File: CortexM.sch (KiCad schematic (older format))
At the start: 8 parts

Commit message: Finish sch without values
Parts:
- added C10, C11, C3, C4, C5, C6, C7, C8, C9: C_Small, symbol Device:C_Small
- added D2: LED, symbol Device:LED
- added J2, J3: Conn_01x15, symbol Connector_Generic:Conn_01x15
- added JP1: SolderJumper_2_Open, symbol Jumper:SolderJumper_2_Open
- added L1: L_Small, symbol Device:L_Small
- added R2, R3: R_Small, symbol Device:R_Small
- added Y1: Crystal_Small, symbol Device:Crystal_Small
- gave numbers to parts that had none: 8
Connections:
- net +3V3: now also U2.1 (VBAT), U2.24 (VDD), U2.36 (VDD), U2.48 (VDD), C3.1, C4.1, C6.1, C8.1, C9.1, J2.1 (Pin_1), J3.1 (Pin_1), JP1.1 (A), L1.1, R3.1
- net GND: now also U2.23 (VSS), U2.35 (VSS), U2.47 (VSS), U2.8 (VSSA), C10.2, C11.2, C3.2, C4.2, C5.2, C6.2, C7.2, C8.2, C9.2, D2.1 (K), J2.2 (Pin_2), J3.2 (Pin_2), R2.2
- net USB_D+: now also U2.33 (PA12), R3.2
- net USB_D-: now also U2.32 (PA11)
- net LED_STAT: now reaches U2.11 (PA1)
- net LED_STAT: now also D2.2 (A)
- net PA3: now reaches U2.13 (PA3)
- net PA3: now also J3.15 (Pin_15)
- net PA4: now reaches U2.14 (PA4)
- net PA4: now also J3.14 (Pin_14)
- net PA5: now reaches U2.15 (PA5)
- net PA5: now also J3.13 (Pin_13)
- net PA6: now reaches U2.16 (PA6)
- net PA6: now also J3.12 (Pin_12)
- net PA7: now reaches U2.17 (PA7)
- net PA7: now also J3.11 (Pin_11)
- net PB0: now reaches U2.18 (PB0)
- net PB0: now also J3.10 (Pin_10)
- net PB1: now reaches U2.19 (PB1)
- net PB1: now also J3.9 (Pin_9)
- net PC13: now reaches U2.2 (PC13)
- net PC13: now also J2.13 (Pin_13)
- net PB2: now reaches U2.20 (PB2)
- net PB2: now also J3.8 (Pin_8)
- net PB10: now reaches U2.21 (PB10)
- net PB10: now also J3.7 (Pin_7)
- net PB11: now reaches U2.22 (PB11)
- net PB11: now also J3.6 (Pin_6)
- net PA8: now reaches U2.29 (PA8)
- net PA8: now also J3.5 (Pin_5)
- net PC14: now reaches U2.3 (PC14)
- net PC14: now also J2.14 (Pin_14)
- net PA9: now reaches U2.30 (PA9)
- net PA9: now also J3.4 (Pin_4)
- net PA10: now reaches U2.31 (PA10)
- net PA10: now also J3.3 (Pin_3)
- net SWDIO: now reaches U2.34 (PA13)
- net SWDIO: now also J2.3 (Pin_3)
- net SWCLK: now reaches U2.37 (PA14)
- net SWCLK: now also J2.4 (Pin_4)
- net PA15: now reaches U2.38 (PA15)
- net PA15: now also J2.5 (Pin_5)
- net SWO: now reaches U2.39 (PB3)
- net SWO: now also J2.6 (Pin_6)
- net PC15: now reaches U2.4 (PC15)
- net PC15: now also J2.15 (Pin_15)
- net PB4: now reaches U2.40 (PB4)
- net PB4: now also J2.7 (Pin_7)
- net PB5: now reaches U2.41 (PB5)
- net PB5: now also J2.8 (Pin_8)
- net PB6: now reaches U2.42 (PB6)
- net PB6: now also J2.9 (Pin_9)
- net PB7: now reaches U2.43 (PB7)
- net PB7: now also J2.10 (Pin_10)
- net at U2.44 (BOOT0): now also JP1.2 (B), R2.1
- net PB8: now reaches U2.45 (PB8)
- net PB8: now also J2.11 (Pin_11)
- net PB9: now reaches U2.46 (PB9)
- net PB9: now also J2.12 (Pin_12)
- net at U2.5 (PD0): now also C5.1, Y1.1
- net at U2.6 (PD1): now also C7.1, Y1.2
- net +3.3VA: now reaches U2.9 (VDDA)
- net +3.3VA: now also C10.1, C11.1, L1.2
- no-connect marks 2 -> 9
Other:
- note added: "'Light' low-pass filter for analog VDD"
- note added: "1x bulk decoupling + 100nF per VDD pin"
- note added: "BOOT0:\n1 = BOOTLOADER, 0='RUN'"
- note added: "CL = 2 * (Cload - Cstray)"
- note added: "GPIO HEADERS"
- note added: "STM32F1 Microcontroller"
- note added: "STM32F103"
- moved on the sheet: C1, C2, D1, FB1, J1, R1, U1, U2

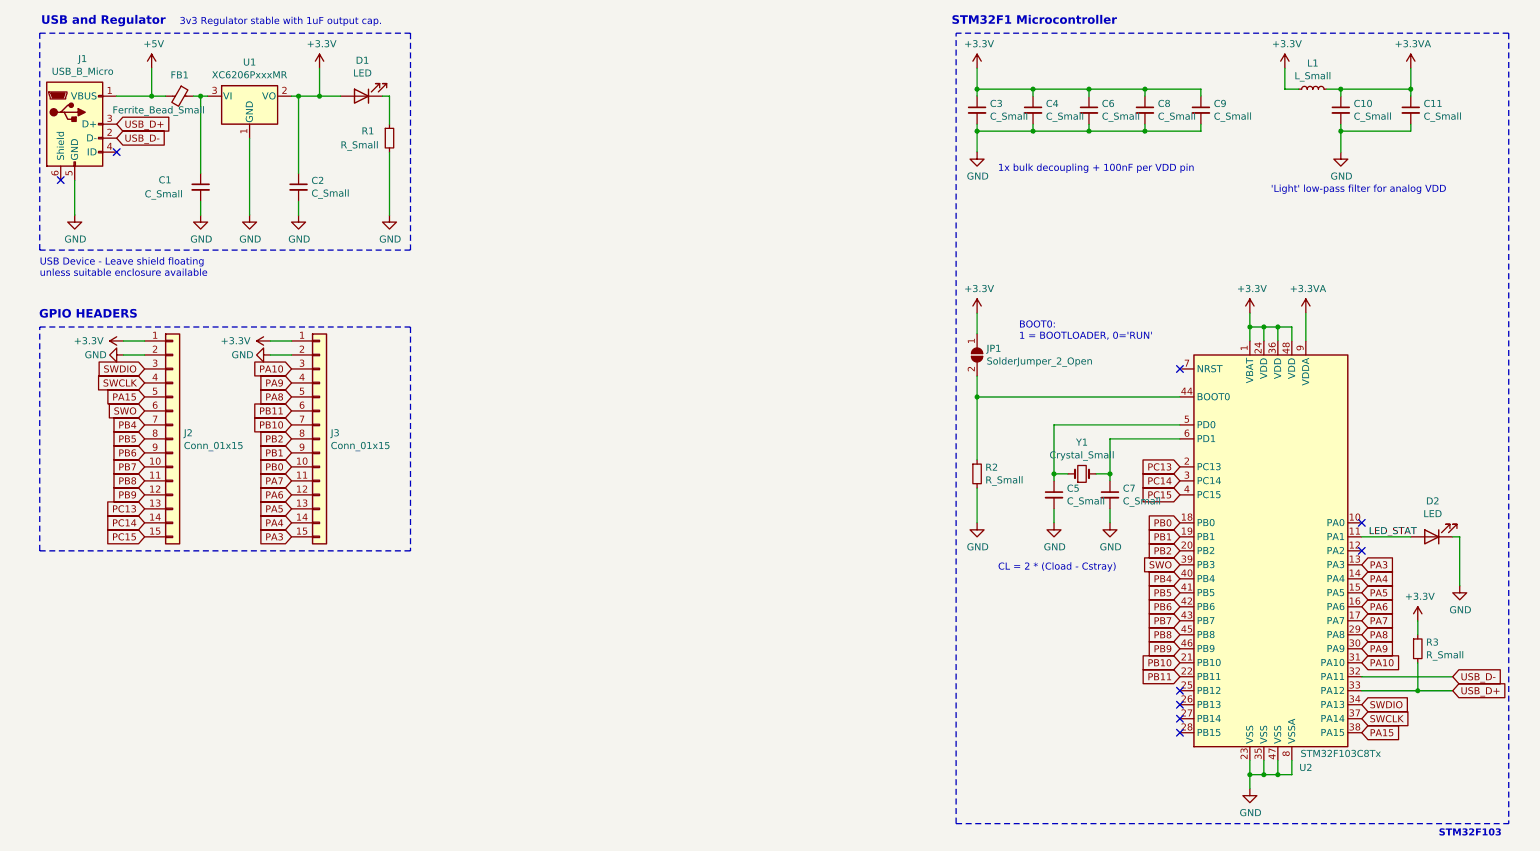
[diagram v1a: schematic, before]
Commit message: Added R4, Added values to sch
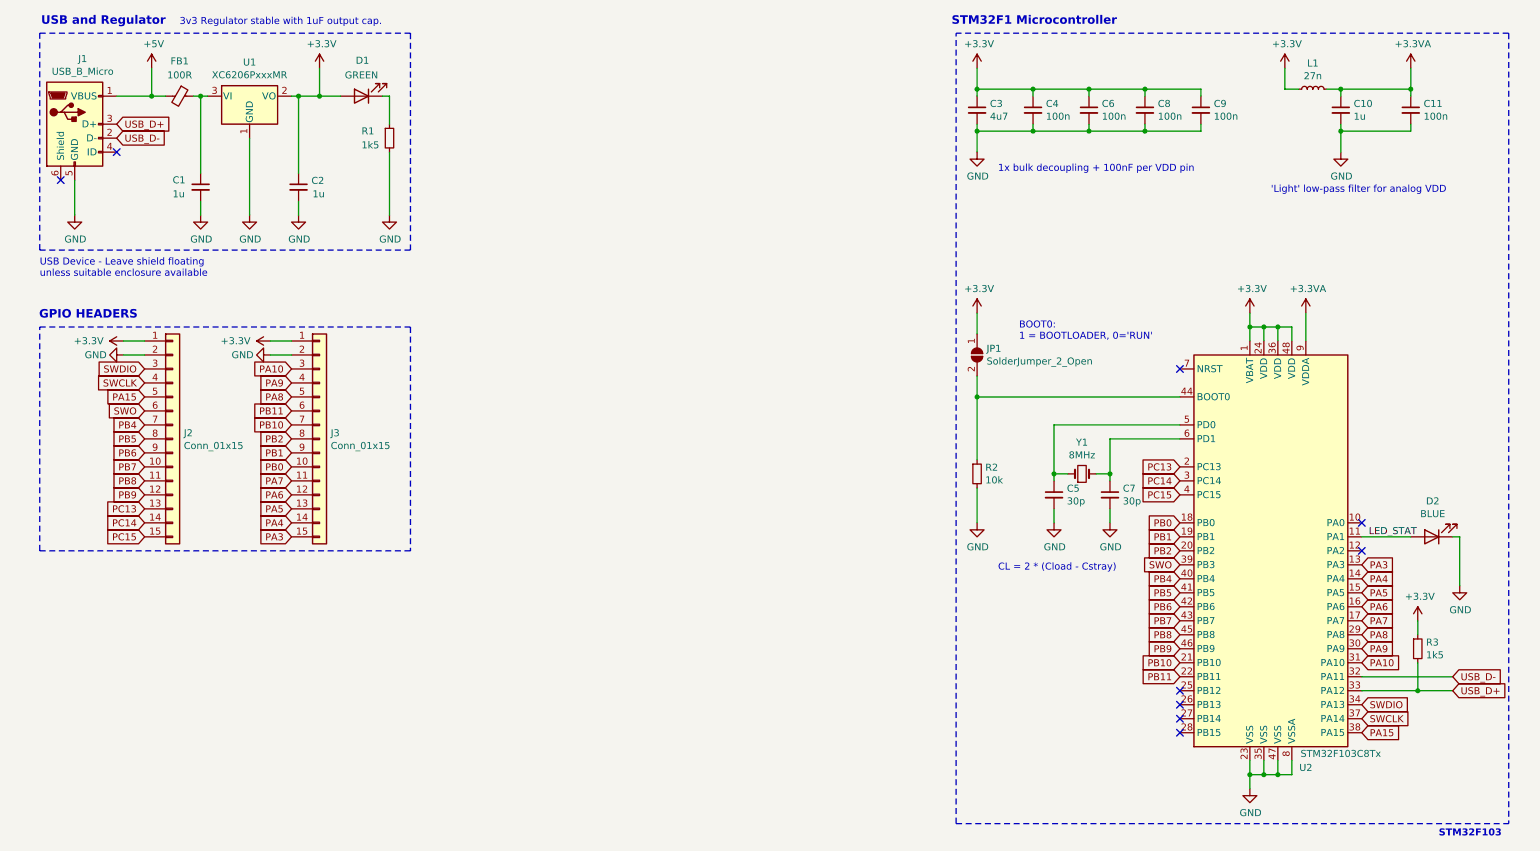
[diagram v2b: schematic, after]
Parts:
- C1, C10, C2: value C_Small -> 1u
- C11, C4, C6, C8, C9: value C_Small -> 100n
- C3: value C_Small -> 4u7
- C5, C7: value C_Small -> 30p
- D1: value LED -> GREEN
- D2: value LED -> BLUE
- FB1: value Ferrite_Bead_Small -> 100R
- L1: value L_Small -> 27n
- R1, R3: value R_Small -> 1k5
- R2: value R_Small -> 10k
- Y1: value Crystal_Small -> 8MHz
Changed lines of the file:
@@
 U 1 1 5FBCDDBD
 P 1600 1150
-F 0 "FB1" V 1450 1150 50  0000 C CNN
-F 1 "Ferrite_Bead_Small" V 1700 1000 50  0000 C CNN
+F 0 "FB1" V 1350 1150 50  0000 C CNN
+F 1 "100R" V 1450 1150 50  0000 C CNN
 F 2 "" V 1530 1150 50  0001 C CNN
 F 3 "~" H 1600 1150 50  0001 C CNN
@@
 U 1 1 5FBCF834
 P 1750 1800
-F 0 "C1" H 1450 1850 50  0000 L CNN
-F 1 "C_Small" H 1350 1750 50  0000 L CNN
+F 0 "C1" H 1550 1850 50  0000 L CNN
+F 1 "1u" H 1550 1750 50  0000 L CNN
 F 2 "" H 1750 1800 50  0001 C CNN
 F 3 "~" H 1750 1800 50  0001 C CNN
@@
 P 2450 1800
 F 0 "C2" H 2542 1846 50  0000 L CNN
-F 1 "C_Small" H 2542 1755 50  0000 L CNN
+F 1 "1u" H 2550 1750 50  0000 L CNN
 F 2 "" H 2450 1800 50  0001 C CNN
 F 3 "~" H 2450 1800 50  0001 C CNN
@@
 P 3100 1450
 F 0 "R1" H 2900 1500 50  0000 L CNN
-F 1 "R_Small" H 2750 1400 50  0000 L CNN
+F 1 "1k5" H 2900 1400 50  0000 L CNN
 F 2 "" H 3100 1450 50  0001 C CNN
 F 3 "~" H 3100 1450 50  0001 C CNN
@@
 P 2900 1150
 F 0 "D1" H 2893 895 50  0000 C CNN
-F 1 "LED" H 2893 986 50  0000 C CNN
+F 1 "GREEN" H 2900 1000 50  0000 C CNN
 F 2 "" H 2900 1150 50  0001 C CNN
 F 3 "~" H 2900 1150 50  0001 C CNN
@@
 P 10550 4300
 F 0 "D2" H 10543 4045 50  0000 C CNN
-F 1 "LED" H 10543 4136 50  0000 C CNN
+F 1 "BLUE" H 10543 4136 50  0000 C CNN
 F 2 "" H 10550 4300 50  0001 C CNN
 F 3 "~" H 10550 4300 50  0001 C CNN
@@
 P 10450 5100
 F 0 "R3" H 10509 5146 50  0000 L CNN
-F 1 "R_Small" H 10509 5055 50  0000 L CNN
+F 1 "1k5" H 10509 5055 50  0000 L CNN
 F 2 "" H 10450 5100 50  0001 C CNN
 F 3 "~" H 10450 5100 50  0001 C CNN
@@
 P 8050 3850
 F 0 "Y1" H 8050 4075 50  0000 C CNN
-F 1 "Crystal_Small" H 8050 3984 50  0000 C CNN
+F 1 "8MHz" H 8050 3984 50  0000 C CNN
 F 2 "" H 8050 3850 50  0001 C CNN
 F 3 "~" H 8050 3850 50  0001 C CNN
@@
 P 7850 4000
 F 0 "C5" H 7942 4046 50  0000 L CNN
-F 1 "C_Small" H 7942 3955 50  0000 L CNN
+F 1 "30p" H 7942 3955 50  0000 L CNN
 F 2 "" H 7850 4000 50  0001 C CNN
 F 3 "~" H 7850 4000 50  0001 C CNN
@@
 P 8250 4000
 F 0 "C7" H 8342 4046 50  0000 L CNN
-F 1 "C_Small" H 8342 3955 50  0000 L CNN
+F 1 "30p" H 8342 3955 50  0000 L CNN
 F 2 "" H 8250 4000 50  0001 C CNN
 F 3 "~" H 8250 4000 50  0001 C CNN
@@
 P 7300 3850
 F 0 "R2" H 7359 3896 50  0000 L CNN
-F 1 "R_Small" H 7359 3805 50  0000 L CNN
+F 1 "10k" H 7359 3805 50  0000 L CNN
 F 2 "" H 7300 3850 50  0001 C CNN
 F 3 "~" H 7300 3850 50  0001 C CNN
@@
 P 7300 1250
 F 0 "C3" H 7392 1296 50  0000 L CNN
-F 1 "C_Small" H 7392 1205 50  0000 L CNN
+F 1 "4u7" H 7392 1205 50  0000 L CNN
 F 2 "" H 7300 1250 50  0001 C CNN
 F 3 "~" H 7300 1250 50  0001 C CNN
@@
 P 7700 1250
 F 0 "C4" H 7792 1296 50  0000 L CNN
-F 1 "C_Small" H 7792 1205 50  0000 L CNN
+F 1 "100n" H 7792 1205 50  0000 L CNN
 F 2 "" H 7700 1250 50  0001 C CNN
 F 3 "~" H 7700 1250 50  0001 C CNN
@@
 P 8100 1250
 F 0 "C6" H 8192 1296 50  0000 L CNN
-F 1 "C_Small" H 8192 1205 50  0000 L CNN
+F 1 "100n" H 8192 1205 50  0000 L CNN
 F 2 "" H 8100 1250 50  0001 C CNN
 F 3 "~" H 8100 1250 50  0001 C CNN
@@
 P 8500 1250
 F 0 "C8" H 8592 1296 50  0000 L CNN
-F 1 "C_Small" H 8592 1205 50  0000 L CNN
+F 1 "100n" H 8592 1205 50  0000 L CNN
 F 2 "" H 8500 1250 50  0001 C CNN
 F 3 "~" H 8500 1250 50  0001 C CNN
@@
 P 8900 1250
 F 0 "C9" H 8992 1296 50  0000 L CNN
-F 1 "C_Small" H 8992 1205 50  0000 L CNN
+F 1 "100n" H 8992 1205 50  0000 L CNN
 F 2 "" H 8900 1250 50  0001 C CNN
 F 3 "~" H 8900 1250 50  0001 C CNN
@@
 P 9900 1250
 F 0 "C10" H 9992 1296 50  0000 L CNN
-F 1 "C_Small" H 9992 1205 50  0000 L CNN
+F 1 "1u" H 9992 1205 50  0000 L CNN
 F 2 "" H 9900 1250 50  0001 C CNN
 F 3 "~" H 9900 1250 50  0001 C CNN
@@
 P 10400 1250
 F 0 "C11" H 10492 1296 50  0000 L CNN
-F 1 "C_Small" H 10492 1205 50  0000 L CNN
+F 1 "100n" H 10492 1205 50  0000 L CNN
 F 2 "" H 10400 1250 50  0001 C CNN
 F 3 "~" H 10400 1250 50  0001 C CNN
@@
 P 9700 1100
 F 0 "L1" V 9885 1100 50  0000 C CNN
-F 1 "L_Small" V 9794 1100 50  0000 C CNN
+F 1 "27n" V 9794 1100 50  0000 C CNN
 F 2 "" H 9700 1100 50  0001 C CNN
 F 3 "~" H 9700 1100 50  0001 C CNN

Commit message: autosave
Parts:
- added R3: 1k5, symbol Device:R_Small
- renumbered C5 to C10, C7 to C11, C6 to C5, C8 to C6, C9 to C7, C10 to C8, C11 to C9, R3 to R4
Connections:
- net GND: now also R3.2; no longer D2.1 (K)
- new net: D2.1 (K), R3.1
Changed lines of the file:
@@
 L power:GND #PWR025
 U 1 1 5FC229C5
-P 10750 4650
-F 0 "#PWR025" H 10750 4400 50  0001 C CNN
-F 1 "GND" H 10755 4477 50  0000 C CNN
-F 2 "" H 10750 4650 50  0001 C CNN
-F 3 "" H 10750 4650 50  0001 C CNN
-	1    10750 4650
+P 10750 4800
+F 0 "#PWR025" H 10750 4550 50  0001 C CNN
+F 1 "GND" H 10755 4627 50  0000 C CNN
+F 2 "" H 10750 4800 50  0001 C CNN
+F 3 "" H 10750 4800 50  0001 C CNN
+	1    10750 4800
 	1    0    0    -1
 $EndComp
@@
 Wire Wire Line
 	10700 4300 10750 4300
-Wire Wire Line
-	10750 4300 10750 4650
 Text Label 10100 4300 0    50   ~ 0
 LED_STAT
@@
 $EndComp
 $Comp
-L Device:R_Small R3
+L Device:R_Small R4
 U 1 1 5FC2B2BA
 P 10450 5100
-F 0 "R3" H 10509 5146 50  0000 L CNN
+F 0 "R4" H 10509 5146 50  0000 L CNN
 F 1 "1k5" H 10509 5055 50  0000 L CNN
 F 2 "" H 10450 5100 50  0001 C CNN
@@
 $EndComp
 $Comp
-L Device:C_Small C5
+L Device:C_Small C10
 U 1 1 5FC32777
 P 7850 4000
-F 0 "C5" H 7942 4046 50  0000 L CNN
+F 0 "C10" H 7942 4046 50  0000 L CNN
 F 1 "30p" H 7942 3955 50  0000 L CNN
 F 2 "" H 7850 4000 50  0001 C CNN
@@
 $EndComp
 $Comp
-L Device:C_Small C7
+L Device:C_Small C11
 U 1 1 5FC33280
 P 8250 4000
-F 0 "C7" H 8342 4046 50  0000 L CNN
+F 0 "C11" H 8342 4046 50  0000 L CNN
 F 1 "30p" H 8342 3955 50  0000 L CNN
 F 2 "" H 8250 4000 50  0001 C CNN
@@
 $EndComp
 $Comp
-L Device:C_Small C6
+L Device:C_Small C5
 U 1 1 5FC4B8EF
 P 8100 1250
-F 0 "C6" H 8192 1296 50  0000 L CNN
+F 0 "C5" H 8192 1296 50  0000 L CNN
 F 1 "100n" H 8192 1205 50  0000 L CNN
 F 2 "" H 8100 1250 50  0001 C CNN
@@
 $EndComp
 $Comp
-L Device:C_Small C8
+L Device:C_Small C6
 U 1 1 5FC4BC1B
 P 8500 1250
-F 0 "C8" H 8592 1296 50  0000 L CNN
+F 0 "C6" H 8592 1296 50  0000 L CNN
 F 1 "100n" H 8592 1205 50  0000 L CNN
 F 2 "" H 8500 1250 50  0001 C CNN
@@
 $EndComp
 $Comp
-L Device:C_Small C9
+L Device:C_Small C7
 U 1 1 5FC4C042
 P 8900 1250
-F 0 "C9" H 8992 1296 50  0000 L CNN
+F 0 "C7" H 8992 1296 50  0000 L CNN
 F 1 "100n" H 8992 1205 50  0000 L CNN
 F 2 "" H 8900 1250 50  0001 C CNN
@@
 $EndComp
 $Comp
-L Device:C_Small C10
+L Device:C_Small C8
 U 1 1 5FC5FBCC
 P 9900 1250
-F 0 "C10" H 9992 1296 50  0000 L CNN
+F 0 "C8" H 9992 1296 50  0000 L CNN
 F 1 "1u" H 9992 1205 50  0000 L CNN
 F 2 "" H 9900 1250 50  0001 C CNN
@@
 $EndComp
 $Comp
-L Device:C_Small C11
+L Device:C_Small C9
 U 1 1 5FC6028C
 P 10400 1250
-F 0 "C11" H 10492 1296 50  0000 L CNN
+F 0 "C9" H 10492 1296 50  0000 L CNN
 F 1 "100n" H 10492 1205 50  0000 L CNN
 F 2 "" H 10400 1250 50  0001 C CNN
@@
 Text Notes 8300 650  2    61   ~ 12
 STM32F1 Microcontroller
+$Comp
+L Device:R_Small R3
+U 1 1 5FD2F348
+P 10750 4550
+F 0 "R3" H 10809 4596 50  0000 L CNN
+F 1 "1k5" H 10809 4505 50  0000 L CNN
+F 2 "" H 10750 4550 50  0001 C CNN
+F 3 "~" H 10750 4550 50  0001 C CNN
+	1    10750 4550
+	1    0    0    -1
+$EndComp
+Wire Wire Line
+	10750 4450 10750 4300
+Wire Wire Line
+	10750 4800 10750 4650
 $EndSCHEMATC
